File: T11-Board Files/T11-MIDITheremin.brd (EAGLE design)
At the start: 101.6 x 62.2 mm, 100 parts, among them IC1 TL072P, IC2 TL072P, T1 2N3904, T2 2N3904, T3 2N3904, T4 2N3904, T5 2N3904

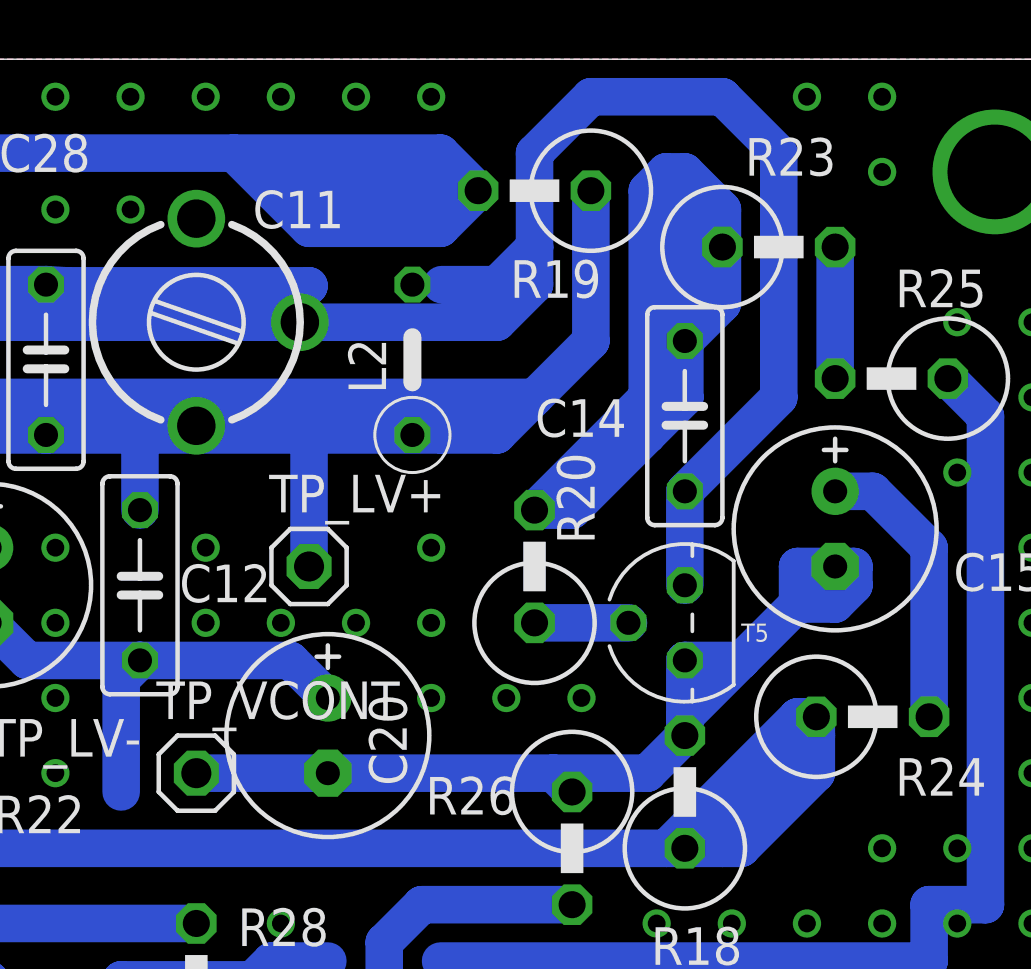
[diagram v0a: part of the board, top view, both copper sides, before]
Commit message: Fixed a couple board issues
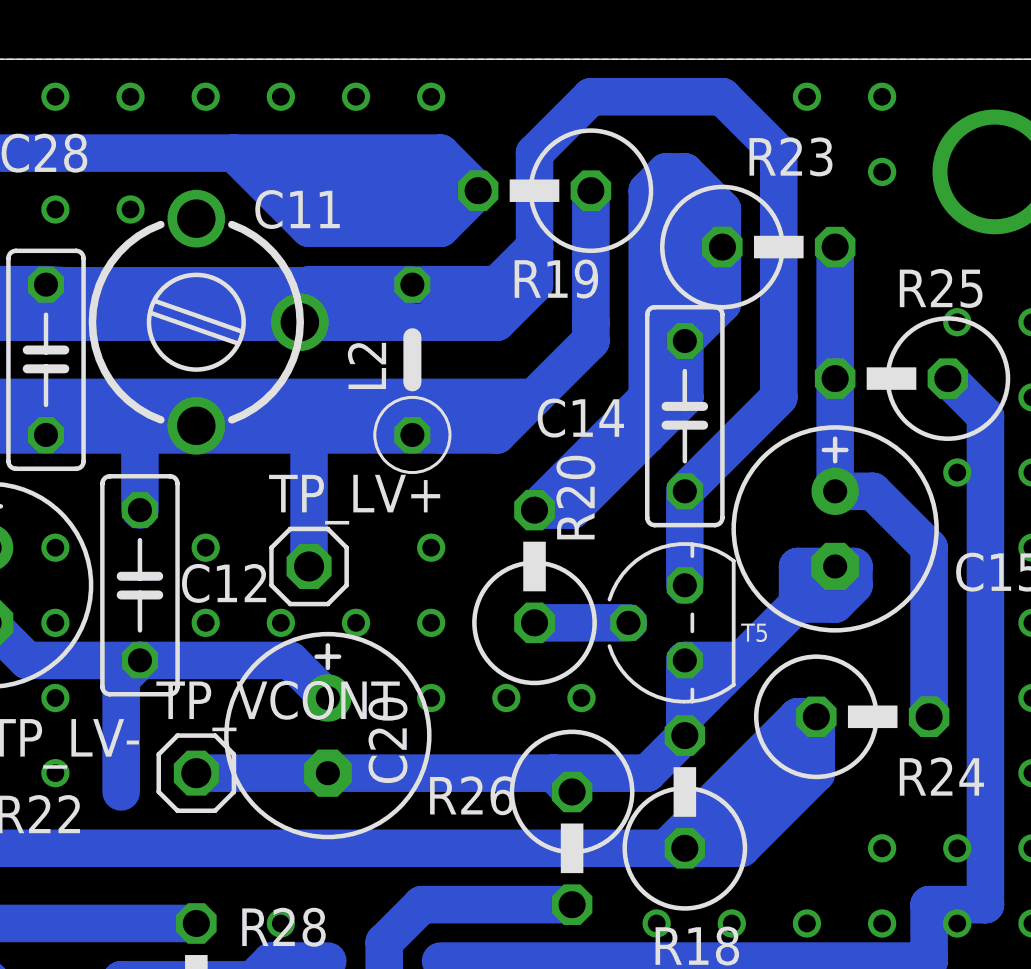
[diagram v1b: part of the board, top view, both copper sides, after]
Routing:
- net L_OSC_V+: track 82.8 -> 90.4 mm
- net LOCAL_RESONANCE: track 120.0 -> 124.2 mm
- net N$23: track 14.1 -> 17.9 mm
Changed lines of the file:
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@@
 <wire x1="68.8975" y1="49.53" x2="70.8025" y2="49.53" width="1.27" layer="16"/>
 <wire x1="70.8025" y1="49.53" x2="74.6125" y2="49.53" width="1.27" layer="16"/>
-<wire x1="74.6125" y1="49.53" x2="79.0175" y2="49.53" width="1.27" layer="16"/>
+<wire x1="74.6125" y1="49.53" x2="78.105" y2="49.53" width="1.27" layer="16"/>
+<wire x1="78.105" y1="49.53" x2="79.0175" y2="49.53" width="1.27" layer="16"/>
 <wire x1="65.7225" y1="49.53" x2="62.5475" y2="49.53" width="1.27" layer="16"/>
 <wire x1="63.8175" y1="45.72" x2="59.3725" y2="45.72" width="1.27" layer="16"/>
@@
 <wire x1="80.9625" y1="49.53" x2="82.2325" y2="50.8" width="1.27" layer="16"/>
 <wire x1="82.2325" y1="50.8" x2="84.1375" y2="52.705" width="1.27" layer="16"/>
-<wire x1="84.1375" y1="52.705" x2="84.1375" y2="57.785" width="1.27" layer="16"/>
+<wire x1="84.1375" y1="52.705" x2="84.1375" y2="53.34" width="1.27" layer="16"/>
+<wire x1="84.1375" y1="53.34" x2="84.1375" y2="57.785" width="1.27" layer="16"/>
 <wire x1="59.3725" y1="49.53" x2="59.3725" y2="50.165" width="1.27" layer="16"/>
 <wire x1="59.3725" y1="50.165" x2="60.0075" y2="50.8" width="1.27" layer="16"/>
 <wire x1="60.0075" y1="50.8" x2="82.2325" y2="50.8" width="1.27" layer="16"/>
 <contactref element="L2" pad="1"/>
-<wire x1="79.0175" y1="49.53" x2="78.105" y2="49.53" width="0" layer="19" extent="16-16"/>
+<wire x1="78.105" y1="49.53" x2="80.3275" y2="49.53" width="0.4064" layer="16"/>
+<wire x1="80.3275" y1="49.53" x2="84.1375" y2="53.34" width="0.4064" layer="16"/>
 </signal>
 <signal name="L_OSC_V-">
@@
 <wire x1="87.3125" y1="40.005" x2="89.2175" y2="41.91" width="1.27" layer="16"/>
 <contactref element="TP_VCONT" pad="1"/>
-<wire x1="70.8025" y1="38.1" x2="82.8675" y2="38.1" width="1.27" layer="16"/>
+<wire x1="70.8025" y1="38.1" x2="75.2475" y2="38.1" width="1.27" layer="16"/>
+<wire x1="75.2475" y1="38.1" x2="82.8675" y2="38.1" width="1.27" layer="16"/>
 <wire x1="82.8675" y1="38.1" x2="83.5025" y2="37.465" width="1.27" layer="16"/>
 <wire x1="87.3125" y1="39.37" x2="86.0425" y2="38.1" width="1.27" layer="16"/>
 <wire x1="86.0425" y1="38.1" x2="82.8675" y2="38.1" width="1.27" layer="16"/>
-<wire x1="70.8025" y1="38.1" x2="75.2475" y2="38.1" width="0" layer="19" extent="1-1"/>
 </signal>
 <signal name="N$21">
@@
 <wire x1="93.6625" y1="47.625" x2="92.3925" y2="47.625" width="1.27" layer="16"/>
 <wire x1="92.3925" y1="55.88" x2="92.3925" y2="51.435" width="1.27" layer="16"/>
-<wire x1="92.3925" y1="47.625" x2="92.3925" y2="51.435" width="0" layer="19" extent="1-1"/>
+<wire x1="92.3925" y1="47.625" x2="92.3925" y2="51.435" width="1.27" layer="16"/>
 </signal>
 <signal name="N$14">
@@
 <wire x1="74.3025" y1="53.34" x2="74.3025" y2="54.26" width="1.27" layer="16"/>
 <wire x1="74.3025" y1="54.26" x2="74.6125" y2="54.57" width="1.27" layer="16"/>
-<wire x1="79.0975" y1="54.61" x2="80.9625" y2="54.61" width="1.27" layer="16"/>
+<wire x1="78.4625" y1="54.61" x2="80.9625" y2="54.61" width="1.27" layer="16"/>
 <wire x1="80.9625" y1="54.61" x2="82.2325" y2="55.88" width="1.27" layer="16"/>
 <wire x1="82.2325" y1="55.88" x2="82.2325" y2="59.055" width="1.27" layer="16"/>
@@
 <wire x1="80.9625" y1="53.34" x2="54.2925" y2="53.34" width="1.27" layer="16"/>
 <contactref element="L2" pad="2"/>
-<wire x1="79.0975" y1="54.61" x2="78.105" y2="54.61" width="0" layer="19" extent="16-16"/>
+<wire x1="78.105" y1="54.61" x2="74.6125" y2="54.61" width="1.27" layer="16"/>
+<wire x1="74.6125" y1="54.61" x2="74.6125" y2="54.57" width="0.4064" layer="16"/>
 </signal>
 <signal name="N$24">
